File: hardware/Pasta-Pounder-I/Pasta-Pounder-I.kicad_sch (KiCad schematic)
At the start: 54 parts, among them CN1 XT30UPB-M, J1 USB_C_Receptacle, J2 Brushed_Motor_1, J3 Brushed_Motor_2, Q1 AO3401A, SW1 RESET-SW, SW2 BOOT-SW, SW3 5.8 ZSPT, U1 DRV8874PWPR, U2 DRV8874PWPR, U4 USBLC6-2P6, U5 ESP32S3W1, U6 SY8113BADC, U7 SY8113BADC

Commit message: Output and MISC work
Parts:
- added D3: RED_LED, symbol Device:LED
- added D4: GREEN_LED, symbol Device:LED
- added J4: ESC_Port, symbol Connector_Generic:Conn_01x03
- added R16, R17: 1KΩ, symbol Device:R
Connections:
- net +3V3: now also R16.2
- net +5V: now also J4.2 (Pin_2)
- net GND: now also D3.1 (K), D4.1 (K), J4.3 (Pin_3)
- net ESC_PWM: now reaches U5.8 (IO15)
- net ESC_PWM: now also J4.1 (Pin_1)
- net LED_MISC: now reaches U5.9 (IO16)
- net LED_MISC: now also R17.2
- new net: D4.2 (A), R17.1
- new net: D3.2 (A), R16.1
- no-connect marks 37 -> 35
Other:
- note added: "LEDs"

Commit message: Finished Initial Schematic
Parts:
- added CN2: B4B-PH-K-S(LF)(SN), lcsc_footprints:C131334_CONN-TH_B4B-PH-K-S, symbol lcsc_imported:B4B-PH-K-S(LF)(SN)
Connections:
- net +3V3: now also CN2.2
- net GND: now also CN2.1
- net UART_RX: now reaches U5.36 (RXD0)
- net UART_RX: now also CN2.4
- net UART_TX: now reaches U5.37 (TXD0)
- net UART_TX: now also CN2.3
- no-connect marks 35 -> 33
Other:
- moved on the sheet: CN1, D4, R17

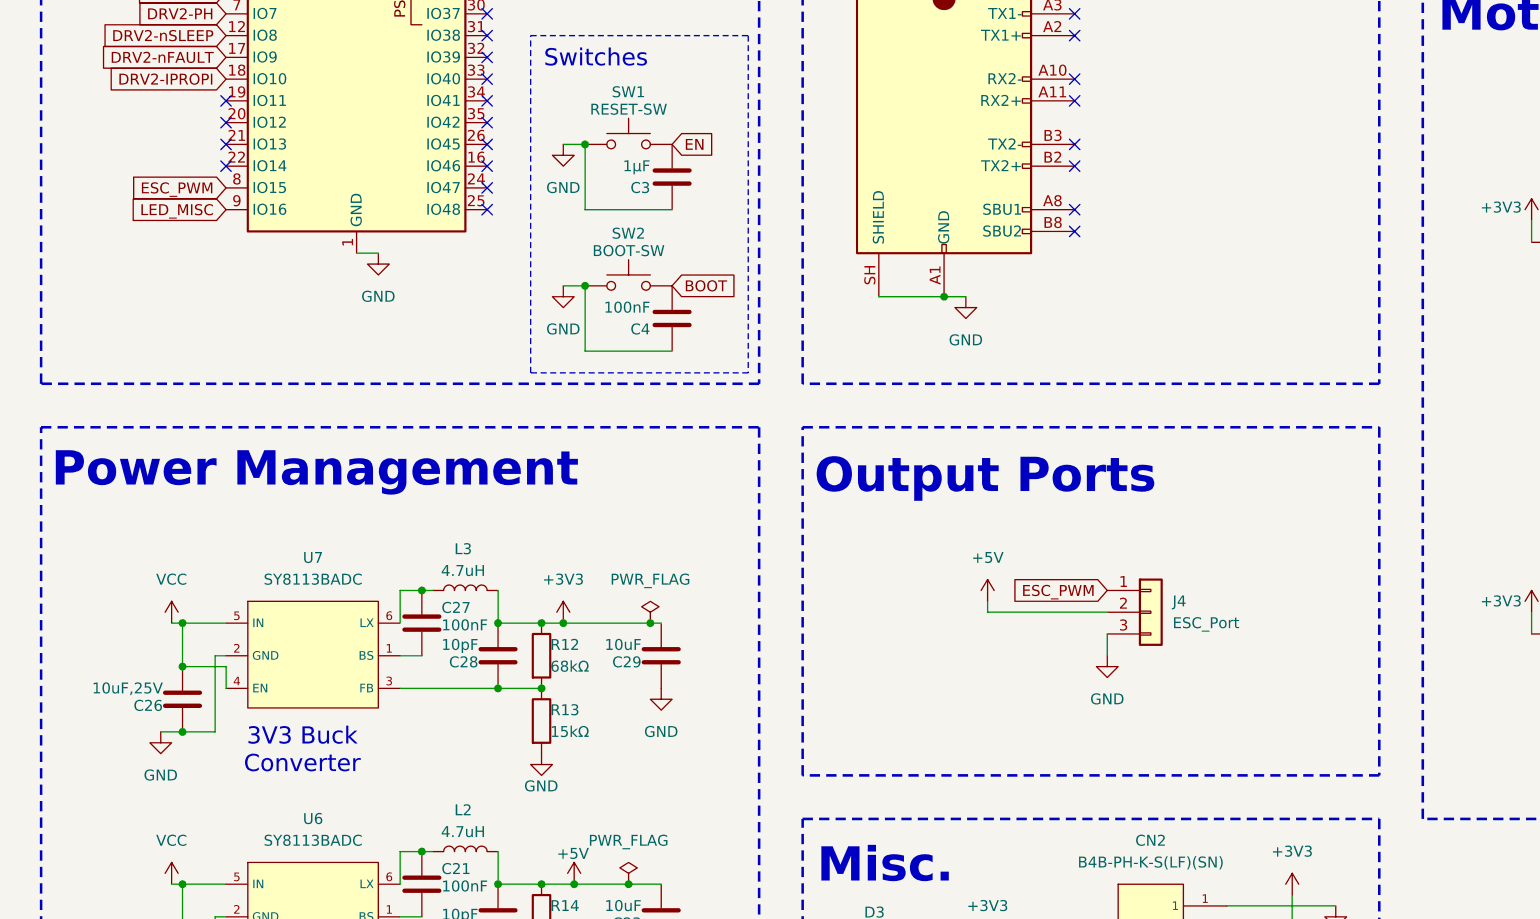
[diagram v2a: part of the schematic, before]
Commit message: Added Flip Servo To Schematic
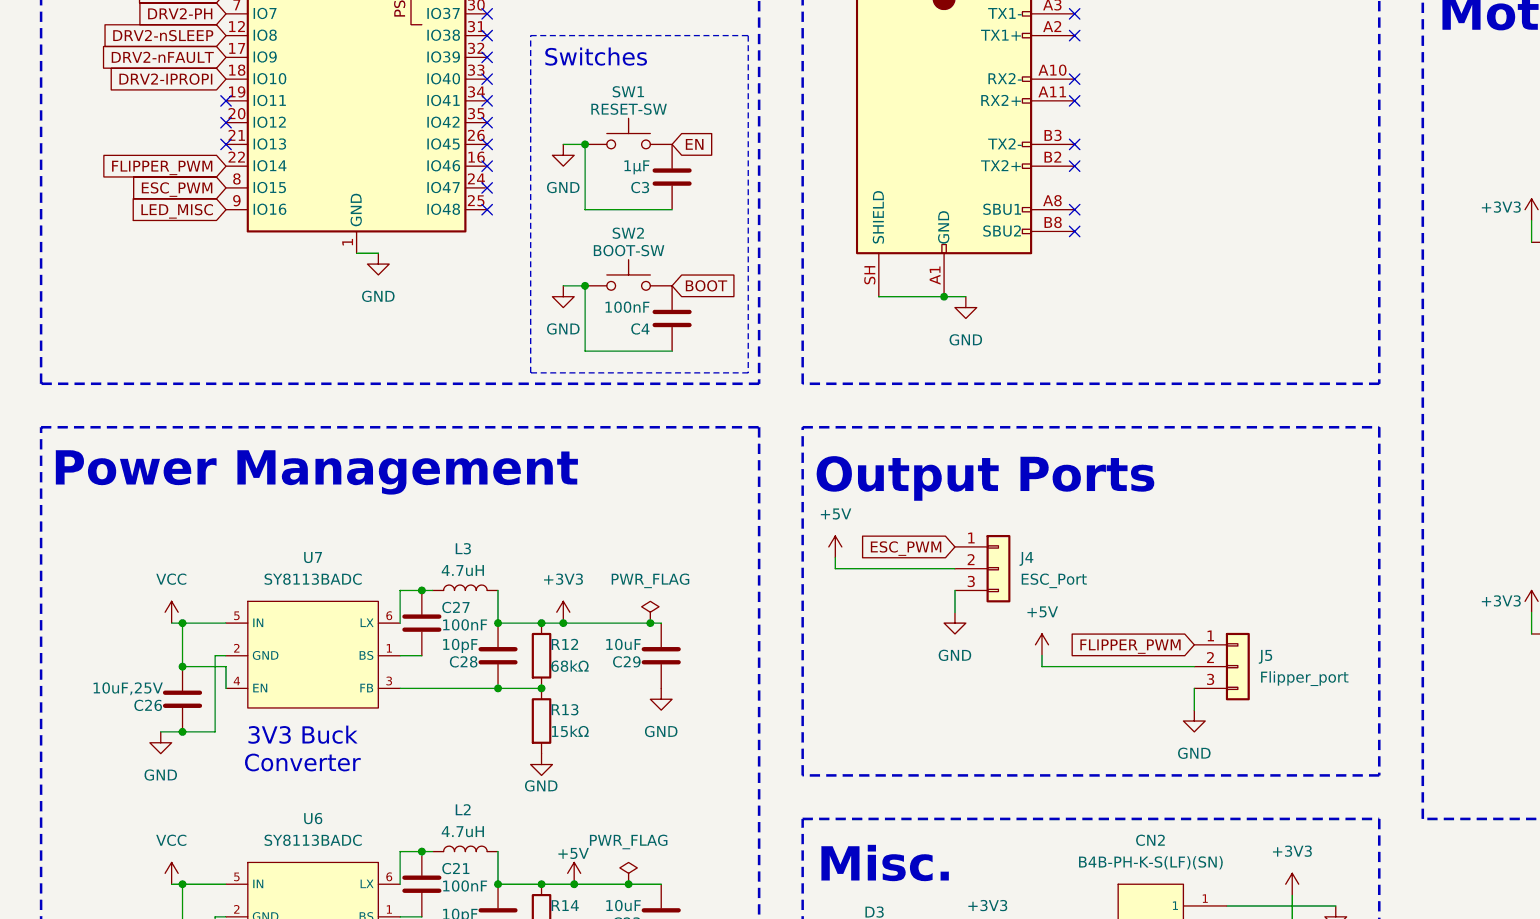
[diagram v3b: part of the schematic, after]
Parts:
- added J5: Flipper_port, symbol Connector_Generic:Conn_01x03
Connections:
- net +5V: now also J5.2 (Pin_2)
- net GND: now also J5.3 (Pin_3)
- net FLIPPER_PWM: now reaches U5.22 (IO14)
- net FLIPPER_PWM: now also J5.1 (Pin_1)
- no-connect marks 33 -> 32
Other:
- moved on the sheet: J4

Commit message: Misc changes
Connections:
- net +5V: no longer J4.2 (Pin_2)
- net VCC: now also J4.2 (Pin_2)
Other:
- note added: "1. Keep the button switches close to the MCU as possible 2. Generally aim for the 470µF caps on the H-Bridges to be large electrolyics 3. Keep good separation between sensitive and high power electronics 3.1. ESCs, Battery in, maybe motor ports, power management etc are all high power 3.2. ESP32, drivers, servo, etc are all sensitive 4. Parts must generally be hot swappable with enough elbow (No 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"
- note added: "Connected Electronics"
- note added: "Extra Robot Information"
- note removed: "https://www.ti.com/lit/ds/symlink/drv8874.pdf?ts=1784644974226"

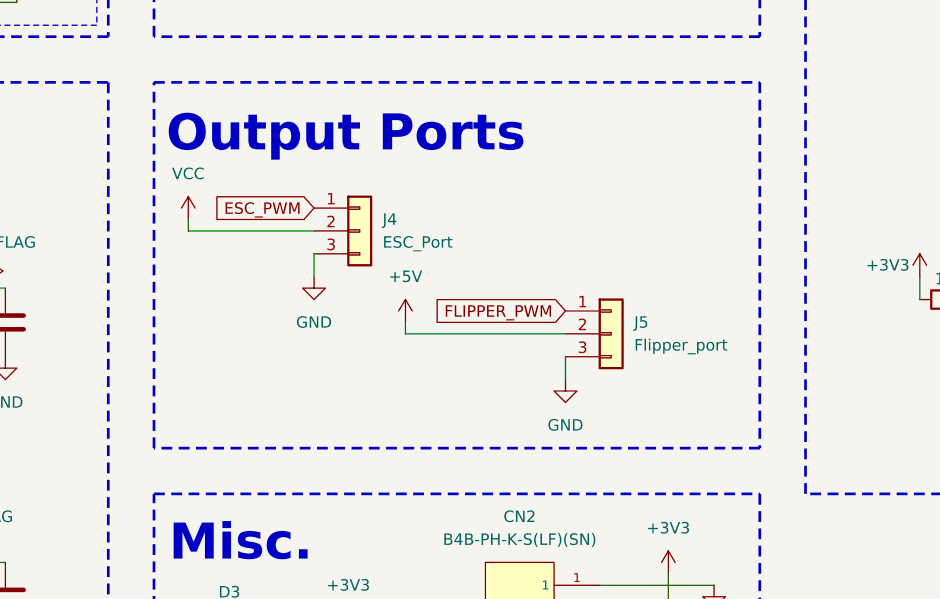
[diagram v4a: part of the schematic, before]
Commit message: Added ESC power terminal
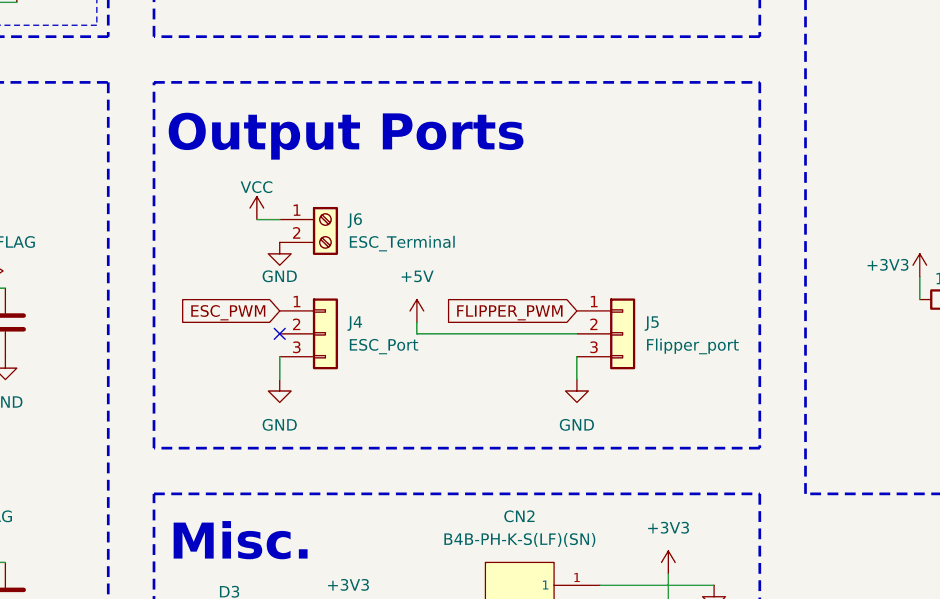
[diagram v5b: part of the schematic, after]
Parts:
- added J6: ESC_Terminal, symbol Connector:Screw_Terminal_01x02
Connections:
- net GND: now also J6.2 (Pin_2)
- net VCC: now also J6.1 (Pin_1); no longer J4.2 (Pin_2)
- no-connect marks 32 -> 33
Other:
- moved on the sheet: J4, J5
